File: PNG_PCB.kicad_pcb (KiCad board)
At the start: 2 copper layers, 129 parts, among them J10 screw term, J11 screw term, J12 screw term, J13 screw term, J14 screw term, J15 screw term, J16 screw term, J17 screw term, J18 screw term, J19 screw term, J2 screw term, J20 screw term, J21 screw term, J22 screw term, J23 screw term, J24 screw term, J25 screw term, J26 screw term, J27 screw term, J28 screw term, J29 screw term, J3 screw term, J30 screw term, J31 screw term, J4 screw term, J5 screw term, J6 screw term, J7 screw term, J8 screw term, J9 screw term, U1 Teensy4.1, U2 Mux, U3 MCP6004, U4 Mux, U5 Mux, U6 MCP6004, U7 Mux, U8 Mux, U9 MCP6004

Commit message: started working on routing the board
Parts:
- moved R52 449.6 mm to (411.8, 217.4)
- moved R62 449.6 mm to (422.9, 240.1)
- moved R63 449.6 mm to (411.8, 247.7)
- moved R7 449.6 mm to (422.9, 247.7)
- moved R72 449.6 mm to (422.9, 232.5)
- moved R79 449.6 mm to (411.8, 240.1)
- moved R81 449.6 mm to (422.9, 224.9)
- moved R16 449.6 mm to (456.3, 247.7)
- moved R17 449.6 mm to (467.4, 232.5)
- moved R18 449.6 mm to (456.3, 240.1)
- moved R25 449.6 mm to (445.1, 247.7)
- moved R26 449.6 mm to (467.4, 224.9)
- moved R27 449.6 mm to (456.3, 232.5)
- moved R34 449.6 mm to (445.1, 240.1)
- moved R35 449.6 mm to (434.0, 247.7)
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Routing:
- added copper zone on F.Cu, net +3V3
- added copper zone on B.Cu, net GND

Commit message: moved sensor r div to other side of mux
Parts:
- removed the R16 at (456.3, 247.7)
- removed the R18 at (456.3, 240.1)
- removed the R25 at (445.1, 247.7)
- removed the R26 at (467.4, 224.9)
- removed the R27 at (456.3, 232.5)
- removed the R34 at (445.1, 240.1)
- removed the R35 at (434.0, 247.7)
- removed the R36 at (467.4, 217.4)
- removed the R43 at (456.3, 224.9)
- removed the R44 at (445.1, 232.5)
- removed the R53 at (456.3, 217.4)
- removed the R54 at (445.1, 224.9)
- removed the R61 at (434.0, 232.5)
- removed the R62 at (422.9, 240.1)
- removed the R63 at (411.8, 247.7)
- removed the R7 at (422.9, 247.7)
- removed the R70 at (445.1, 217.4)
- removed R71, R72, R79, R80, R81, R88, R89, R90: 560, Resistor_THT:R_Axial_DIN0204_L3.6mm_D1.6mm_P5.08mm_Horizontal
- removed the R8 at (467.4, 247.7)
- removed the R9 at (467.4, 240.1)
- added R10: 560, Resistor_THT:R_Axial_DIN0204_L3.6mm_D1.6mm_P5.08mm_Horizontal, F.Cu at (319.8, 116.0)
- added R24: 560, Resistor_THT:R_Axial_DIN0204_L3.6mm_D1.6mm_P5.08mm_Horizontal, F.Cu at (319.8, 123.6)
- added R3: 560, Resistor_THT:R_Axial_DIN0204_L3.6mm_D1.6mm_P5.08mm_Horizontal, F.Cu at (319.8, 108.5)
- added R31: 560, Resistor_THT:R_Axial_DIN0204_L3.6mm_D1.6mm_P5.08mm_Horizontal, F.Cu at (330.9, 116.0)
- added R38: 560, Resistor_THT:R_Axial_DIN0204_L3.6mm_D1.6mm_P5.08mm_Horizontal, F.Cu at (342.0, 108.5)
- added R59: 560, Resistor_THT:R_Axial_DIN0204_L3.6mm_D1.6mm_P5.08mm_Horizontal, F.Cu at (353.1, 108.5)
- added R66: 560, Resistor_THT:R_Axial_DIN0204_L3.6mm_D1.6mm_P5.08mm_Horizontal, F.Cu at (342.0, 123.6)
- moved R17 184.4 mm to (330.9, 108.5)
- moved R45 155.6 mm to (330.9, 123.6)
- moved R52 123.0 mm to (342.0, 116.0)
- renumbered J2 to J1, J11 to J10, J12 to J11, J13 to J12, J14 to J13, J15 to J14, J16 to J15, J17 to J16, J18 to J17, J19 to J18, J20 to J19, J3 to J2, J21 to J20, J22 to J21, J23 to J22, J24 to J23, J25 to J24, J26 to J25, J27 to J26, J28 to J27, J29 to J28, J30 to J29, J4 to J3, J31 to J30, J5 to J4, J6 to J5, J7 to J6, J8 to J7, J9 to J8, J10 to J9, R12 to R11, R13 to R12, R14 to R13, R15 to R14, R19 to R15, R20 to R16, R21 to R18, R22 to R19, R23 to R20, R24 to R21, R28 to R22, R29 to R23, R30 to R25, R31 to R26, R32 to R27, R33 to R28, R37 to R29, R38 to R30, R39 to R32, R40 to R33, R41 to R34, R42 to R35, R46 to R36, R47 to R37, R48 to R39, R3 to R4, R49 to R40, R50 to R41, R51 to R42, R55 to R43, R56 to R44, R57 to R46, R58 to R47, R59 to R48, R60 to R49, R4 to R5, R64 to R50, R65 to R51, R66 to R53, R67 to R54, R68 to R55, R69 to R56, R73 to R57, R74 to R58, R5 to R6, R75 to R60, R76 to R61, R77 to R62, R78 to R63, R82 to R64, R83 to R65, R84 to R67, R85 to R68, R86 to R69, R6 to R7, R87 to R70, R10 to R8, R11 to R9
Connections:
- R17 pad 2: /ampB0/mux1 -> /ampC0/V1
- R45 pad 2: /ampA1/mux2 -> /ampC1/V1
- R52 pad 2: /ampB1/mux0 -> /ampD1/V1

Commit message: organized the mux inputs to their respective muxes
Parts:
- moved J26 302.2 mm to (220.0, 88.4)
- moved J24 299.0 mm to (205.7, 183.9)
- moved J29 297.5 mm to (215.4, 42.4)
- moved J23 282.8 mm to (209.3, 195.6)
- moved J19 280.5 mm to (245.1, 204.2)
- moved J21 266.4 mm to (248.2, 179.8)
- moved J28 264.7 mm to (229.9, 40.1)
- moved J17 259.6 mm to (274.1, 257.6)
- moved J18 259.3 mm to (268.5, 234.7)
- moved J25 247.7 mm to (214.1, 80.3)
- moved J22 246.6 mm to (188.2, 193.8)
- moved J13 244.4 mm to (322.8, 240.3)
- moved U2 242.8 mm to (471.2, 222.5)
- moved J16 226.6 mm to (274.8, 227.3)
- moved J27 226.5 mm to (224.8, 78.7)
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
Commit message: first rough draft for first mux unit
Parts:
- moved R62 206.1 mm to (184.2, 96.3)
- moved R58 196.0 mm to (194.1, 96.0)
- moved R59 135.5 mm to (222.8, 71.6), turned to 180 degrees
- moved R39 121.6 mm to (218.1, 101.5)
- moved R41 121.6 mm to (218.1, 104.7)
- moved R42 121.6 mm to (218.1, 107.8)
- moved R36 121.6 mm to (210.1, 101.5)
- moved R37 121.6 mm to (210.1, 104.7)
- moved R40 121.6 mm to (210.1, 107.8)
- moved R60 61.3 mm to (214.6, 80.5)
- moved R67 47.6 mm to (201.7, 55.1)
- moved J29 38.8 mm to (252.2, 54.6)
- moved J25 38.6 mm to (252.2, 86.4)
- moved R63 36.2 mm to (185.9, 63.5), turned to 180 degrees
- moved J28 35.2 mm to (252.2, 67.3)
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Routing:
- net /ADC_IN_8: track 0.00 -> 65.7 mm
- net /ADC_IN_9: track 0.00 -> 49.4 mm
- net Net-(R60-Pad2): track 0.00 -> 46.5 mm
- net /ampA2/mux0: track 0.00 -> 45.0 mm
- net /ampB2/mux1: track 0.00 -> 39.2 mm
- net /ampA2/mux1: track 0.00 -> 37.3 mm
- net Net-(R61-Pad1): track 0.00 -> 33.1 mm
- net /ampA2/mux2: track 0.00 -> 32.1 mm
- net /ampB2/mux2: track 0.00 -> 30.9 mm
- net Net-(R67-Pad2): track 0.00 -> 30.8 mm
- net /ampB2/mux0: track 0.00 -> 30.1 mm
- net Net-(R68-Pad1): track 0.00 -> 23.4 mm
- net /ampB2/V1: track 0.00 -> 22.2 mm
- net /ampA2/V1: track 0.00 -> 14.5 mm
- net /ampA2/V2: track 0.00 -> 13.9 mm
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
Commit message: one amp setup
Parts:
- moved R44 292.2 mm to (158.2, 141.2)
- moved R49 281.5 mm to (168.4, 141.2)
- moved R43 281.1 mm to (163.3, 145.0), turned to 180 degrees
- moved R47 280.2 mm to (163.3, 148.8), turned to 180 degrees
- moved R46 275.2 mm to (168.4, 145.0)
- moved R48 274.4 mm to (168.4, 148.8)
- moved R55 215.9 mm to (183.6, 148.8), turned to 180 degrees
- moved R53 212.5 mm to (183.6, 145.0), turned to 180 degrees
- moved R50 206.5 mm to (188.7, 145.0)
- moved R56 203.6 mm to (183.6, 141.2), turned to 180 degrees
- moved R54 201.4 mm to (188.7, 148.8)
- moved R51 196.4 mm to (193.8, 141.2), turned to 180 degrees
- moved R32 129.6 mm to (183.6, 122.2), turned to 180 degrees
- moved R35 127.4 mm to (183.6, 126.0), turned to 180 degrees
- moved R34 123.6 mm to (183.6, 118.4), turned to 180 degrees
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
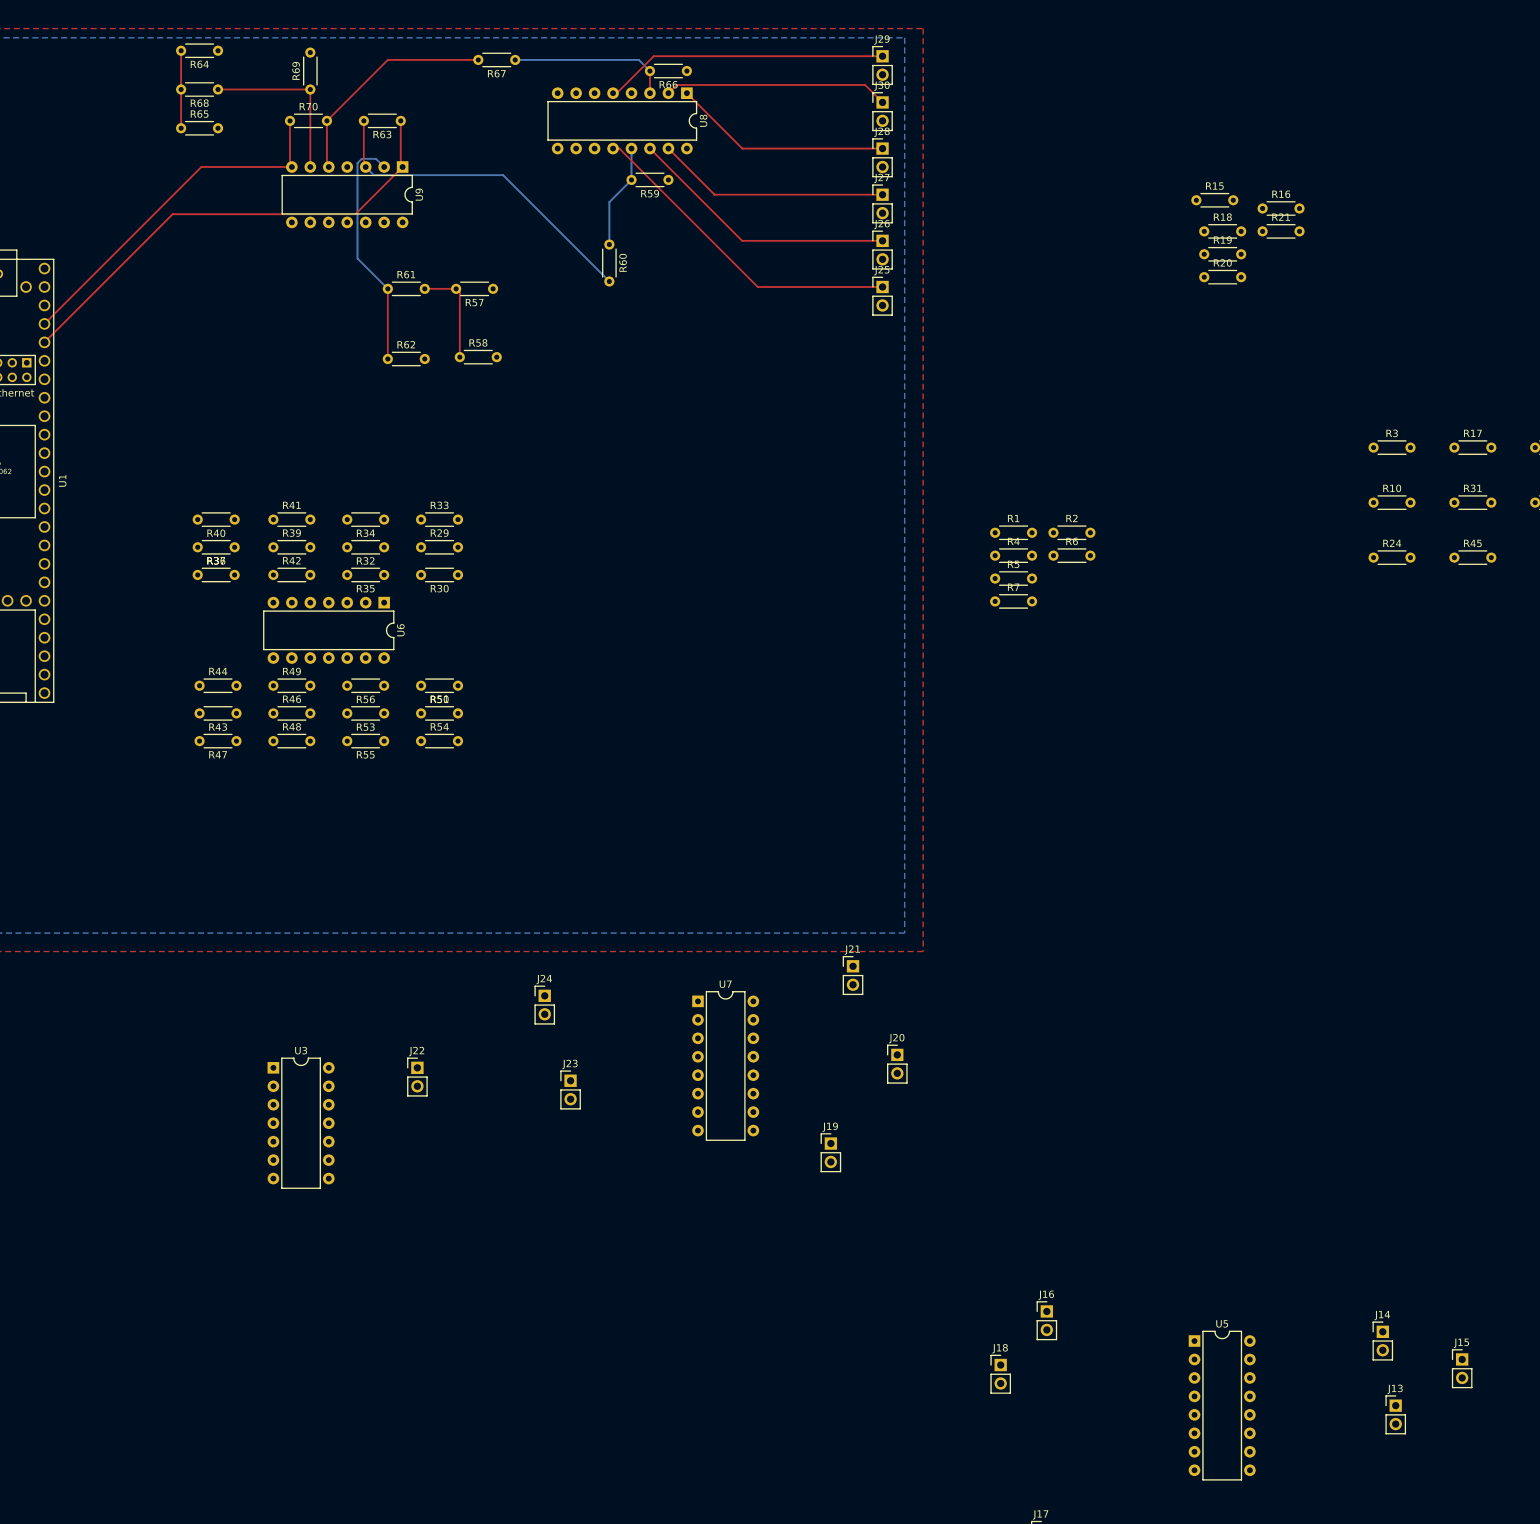
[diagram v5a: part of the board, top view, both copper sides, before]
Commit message: top mux and two amps connected up
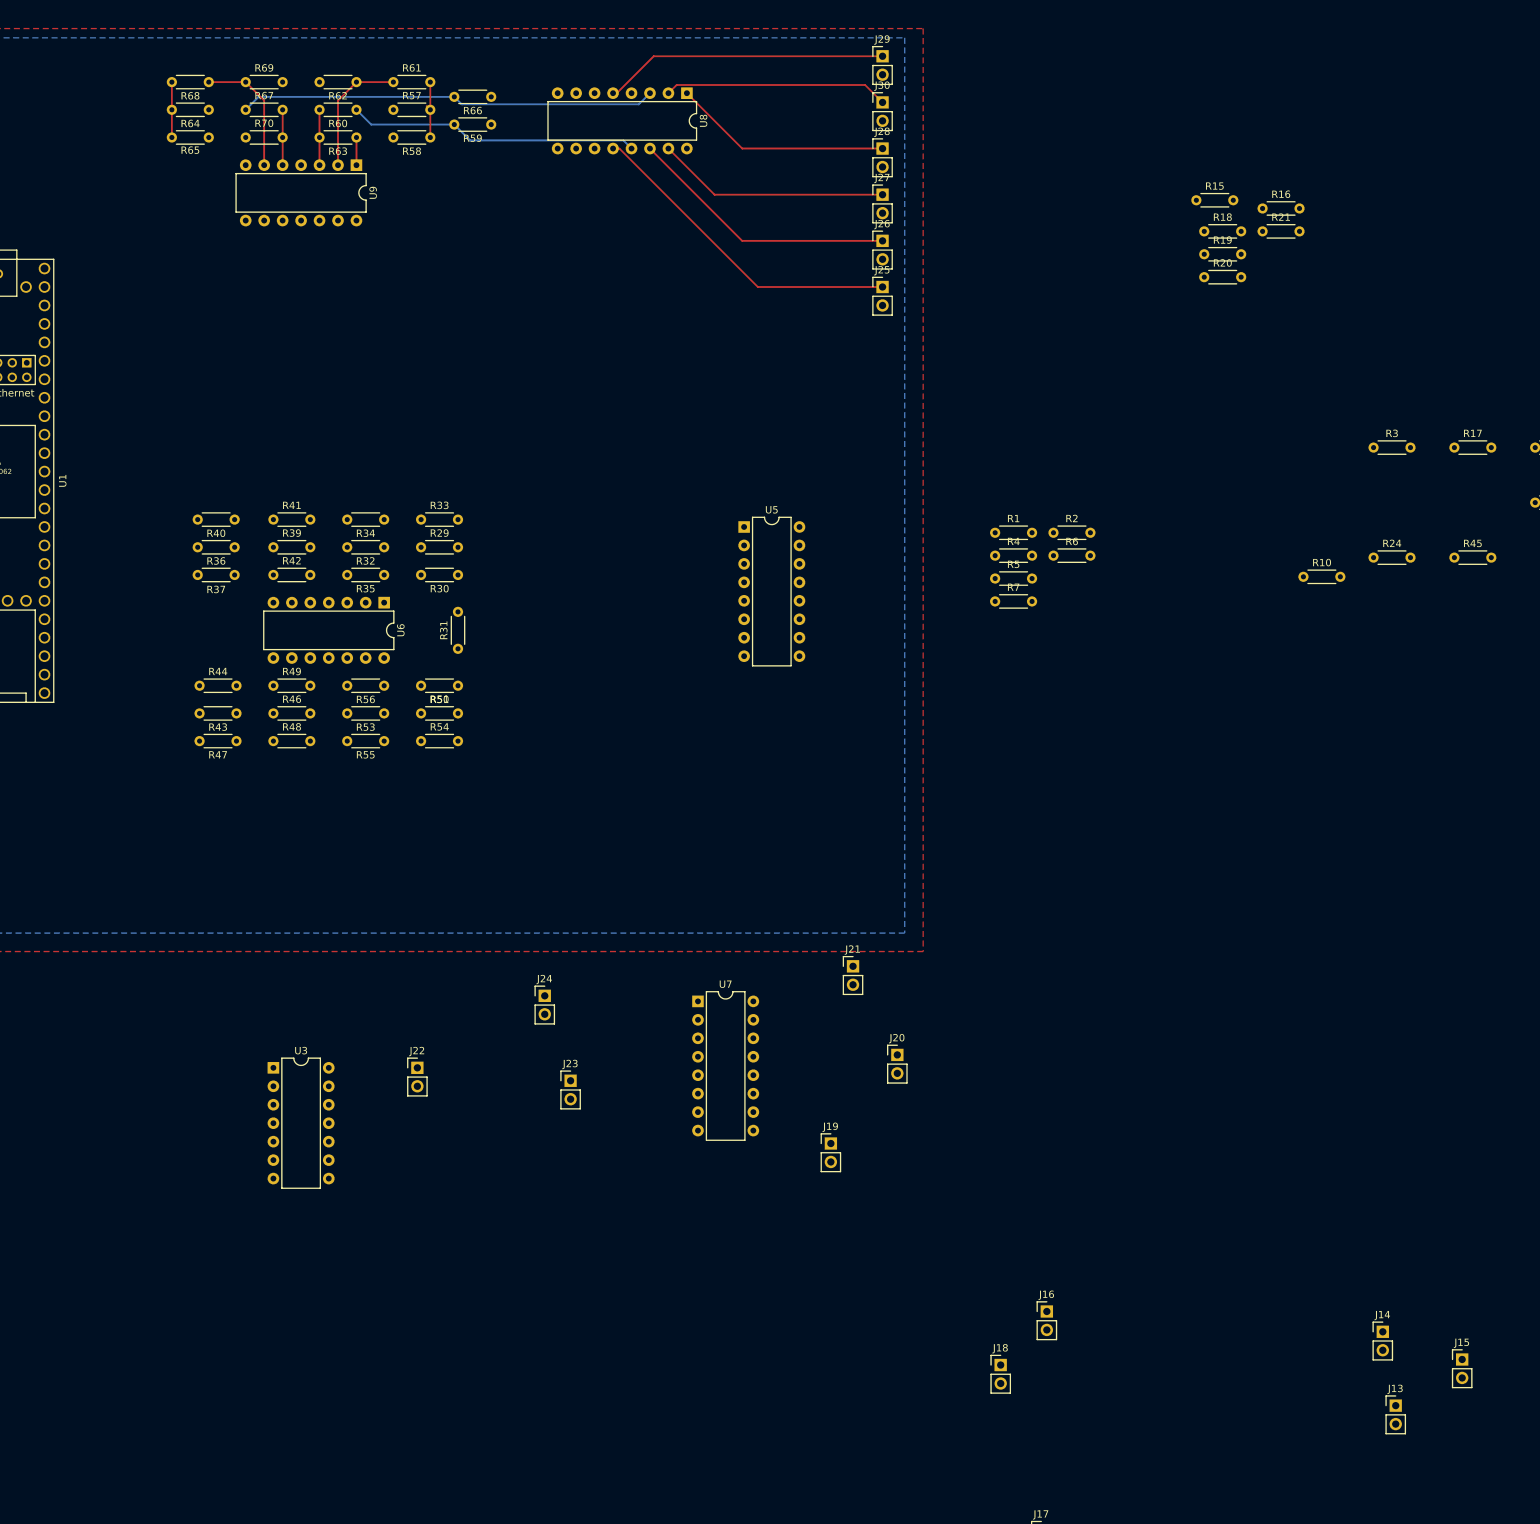
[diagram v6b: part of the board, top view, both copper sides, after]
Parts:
- moved R31 138.6 mm to (193.8, 136.1), turned to 90 degrees
- moved U5 128.0 mm to (233.2, 119.4)
- moved R60 39.4 mm to (179.8, 62.0), turned to 180 degrees
- moved R62 38.3 mm to (179.8, 58.2), turned to 180 degrees
- moved R67 37.7 mm to (164.6, 62.0), turned to 0 degrees
- moved R58 30.5 mm to (190.0, 65.8), turned to 180 degrees
- moved R61 28.5 mm to (184.9, 58.2)
- moved R57 28.2 mm to (184.9, 62.0), turned to 0 degrees
- moved R66 27.2 mm to (198.4, 60.2)
- moved R59 25.5 mm to (198.4, 64.0)
- moved R10 14.1 mm to (310.1, 126.2)
- moved R69 8.95 mm to (164.6, 58.2), turned to 0 degrees
- moved R64 8.23 mm to (159.5, 62.0)
- moved R63 6.51 mm to (179.8, 65.8)
- moved R70 6.51 mm to (164.6, 65.8)
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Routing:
- net /ADC_IN_8: track 65.7 -> 3.81 mm
- net /ADC_IN_9: track 49.4 -> 0.00 mm
- net Net-(R60-Pad2): track 46.5 -> 7.62 mm
- net /ampB2/V1: track 22.2 -> 57.4 mm
- net /ampA2/V1: track 14.5 -> 40.1 mm
- net Net-(R67-Pad2): track 30.8 -> 7.98 mm
- net Net-(R61-Pad1): track 33.1 -> 17.6 mm
- net Net-(R68-Pad1): track 23.4 -> 17.6 mm
- net /ampA2/V2: track 13.9 -> 8.34 mm
- net /ampB2/V2: track 10.7 -> 7.62 mm
